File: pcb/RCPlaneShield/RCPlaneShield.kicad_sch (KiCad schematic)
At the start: 32 parts, among them J1 Roll-D12, J10 Batt Meas-A0, J11 NavLed-D13, J12 NRF24L01 Direct, J13 NRF24L01, J2 Pitch-D11, J3 Yaw-D10, J4 Flaps-D9, J5 Nose Gear-D8, J6 L-Gear-D7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

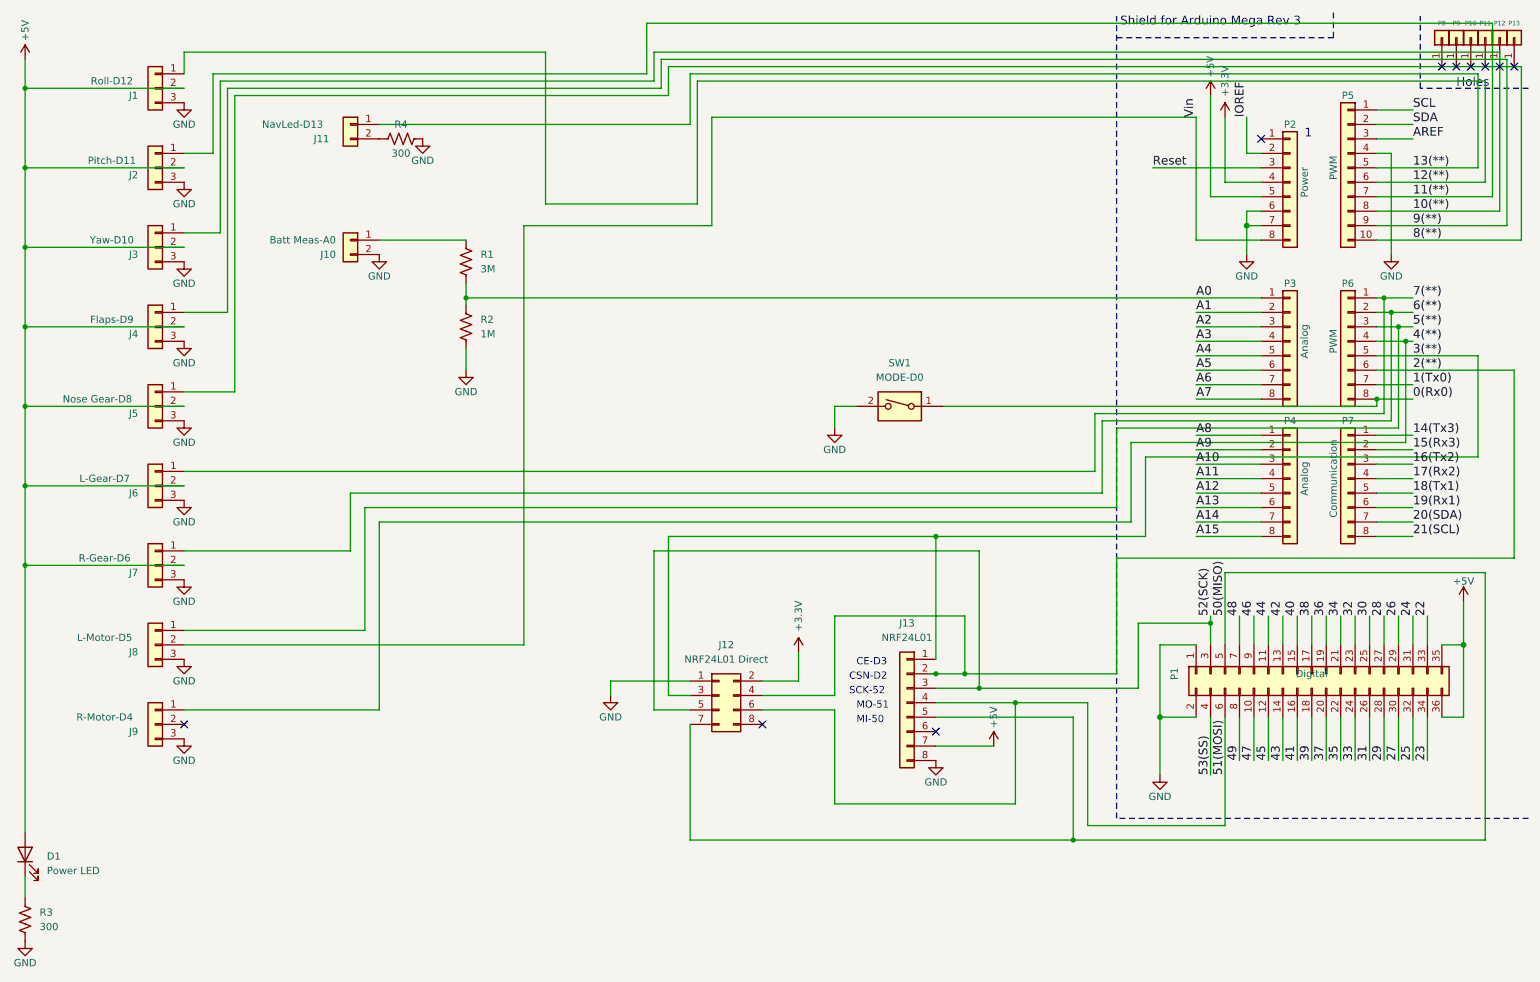
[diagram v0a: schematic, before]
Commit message: Update pcb to v1.1 - wider servo traces, BEC drives servos
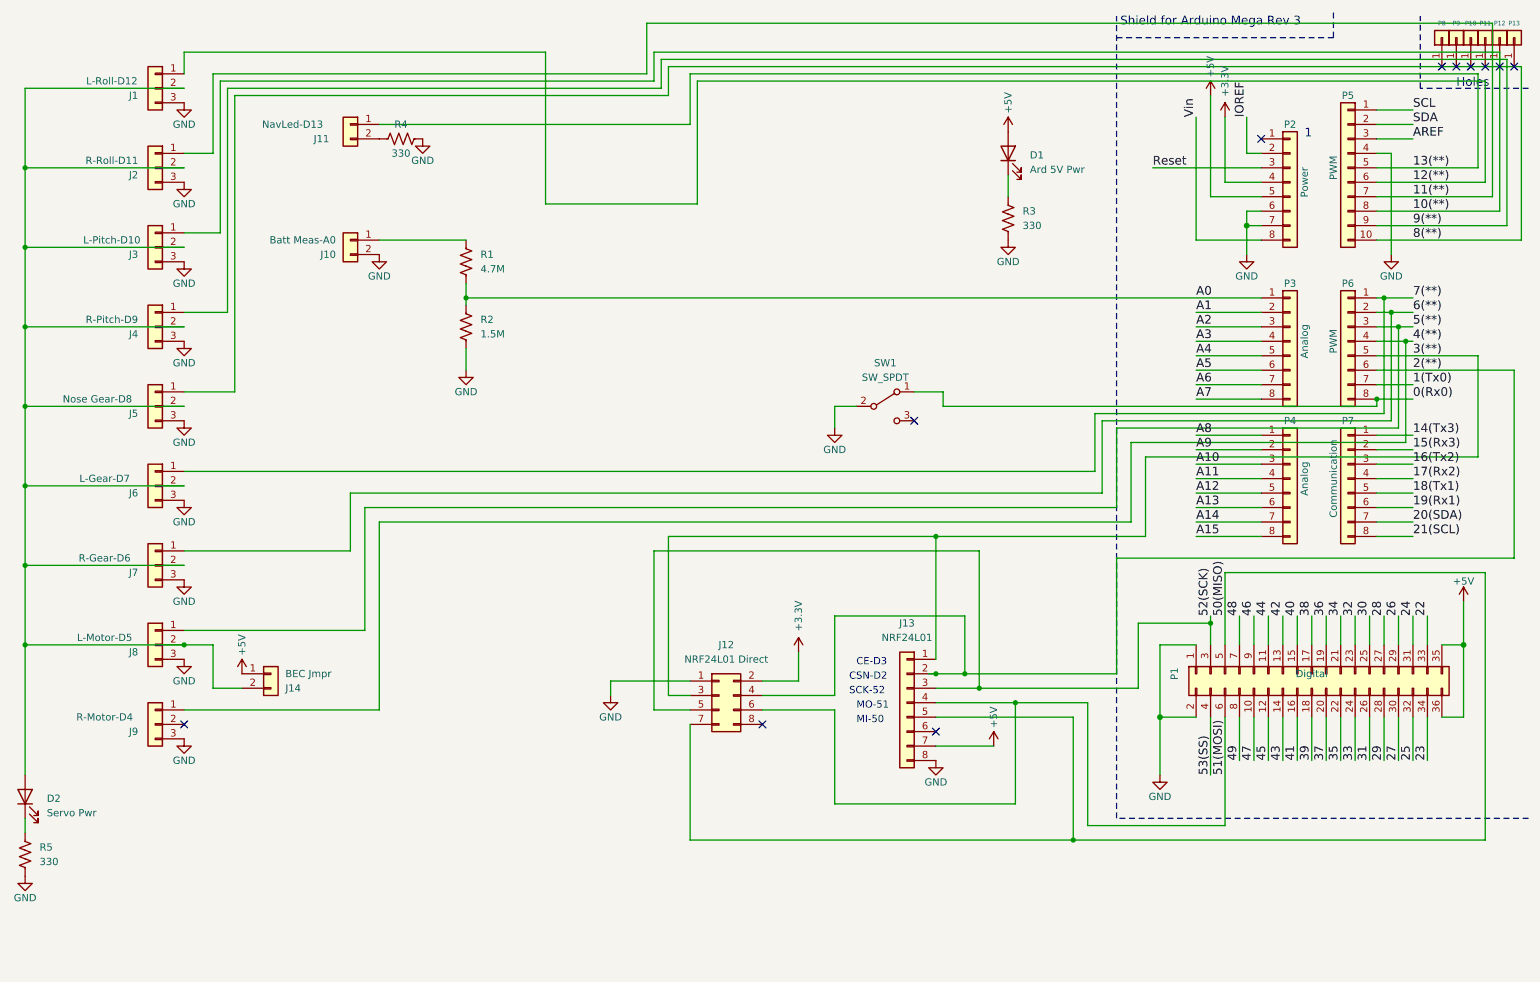
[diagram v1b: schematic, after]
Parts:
- removed SW1: MODE-D0, Button_Switch_THT:SW_DIP_SPSTx01_Slide_9.78x4.72mm_W7.62mm_P2.54mm, symbol Switch:SW_DIP_x01
- added D2: Servo Pwr, LED_THT:LED_D5.0mm, symbol Device:LED
- added J14: BEC Jmpr, Connector_PinHeader_2.54mm:PinHeader_1x02_P2.54mm_Vertical, symbol Connector_Generic:Conn_01x02
- added R5: 330, Resistor_THT:R_Axial_DIN0309_L9.0mm_D3.2mm_P12.70mm_Horizontal, symbol Device:R_US
- added SW1: SW_SPDT, Button_Switch_THT:SW_Slide_1P2T_CK_OS102011MS2Q, symbol Switch:SW_SPDT
- D1: value Power LED -> Ard 5V Pwr
- J1: value Roll-D12 -> L-Roll-D12
- J2: value Pitch-D11 -> R-Roll-D11
- J3: value Yaw-D10 -> L-Pitch-D10
- J4: value Flaps-D9 -> R-Pitch-D9
- R1: value 3M -> 4.7M
- R2: value 1M -> 1.5M
- R3, R4: value 300 -> 330
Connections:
- net +5V: now also J14.1 (Pin_1); no longer J1.2 (Pin_2), J2.2 (Pin_2), J3.2 (Pin_2), J4.2 (Pin_2), J5.2 (Pin_2), J6.2 (Pin_2), J7.2 (Pin_2)
- net 0(Rx0): now also SW1.1 (A)
- net GND: now also R5.2, SW1.2 (B)
- net Vin: no longer J8.2 (Pin_2)
- new net: D2.2 (A), J1.2 (Pin_2), J14.2 (Pin_2), J2.2 (Pin_2), J3.2 (Pin_2), J4.2 (Pin_2), J5.2 (Pin_2), J6.2 (Pin_2), J7.2 (Pin_2), J8.2 (Pin_2)
- new net: D2.1 (K), R5.1
- no-connect marks 10 -> 11
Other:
- moved on the sheet: D1, R3
